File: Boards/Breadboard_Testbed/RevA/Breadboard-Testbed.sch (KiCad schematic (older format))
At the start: 13 parts, among them J1 main_conn_10, J10 Arduino-right, J11 Arduino-right, J12 Conn_02x12_Counter_Clockwise, J2 main_conn_12, J3 Conn_02x10_Counter_Clockwise, J4 Conn_02x10_Counter_Clockwise, J5 Conn_02x10_Counter_Clockwise, J6 Arduino-left, J7 Arduino-left, J8 Conn_02x10_Counter_Clockwise, J9 Conn_02x12_Counter_Clockwise

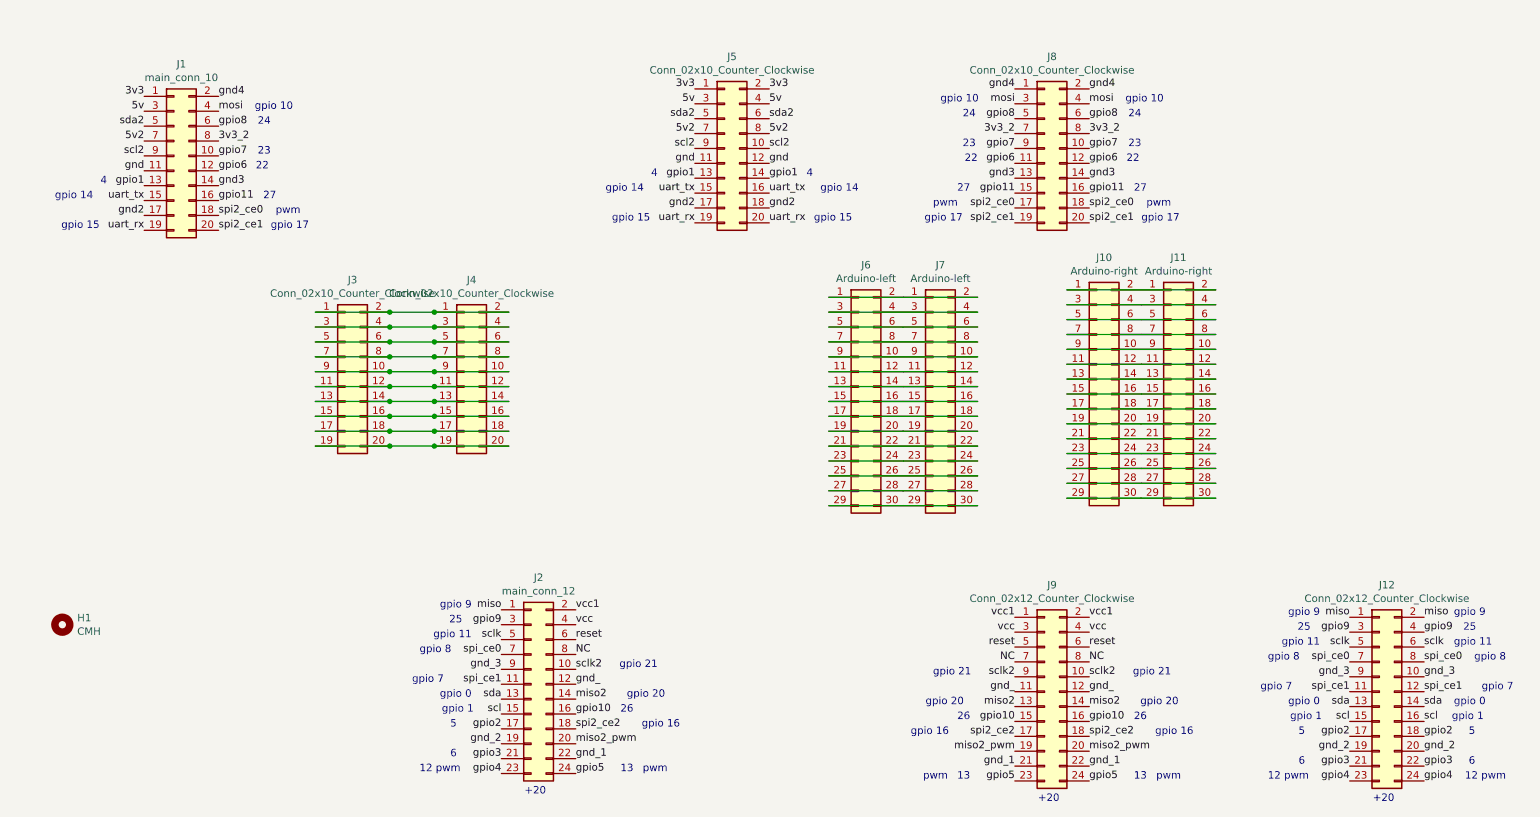
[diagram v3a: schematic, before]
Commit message: Finished Test-RevA layout Pre-route
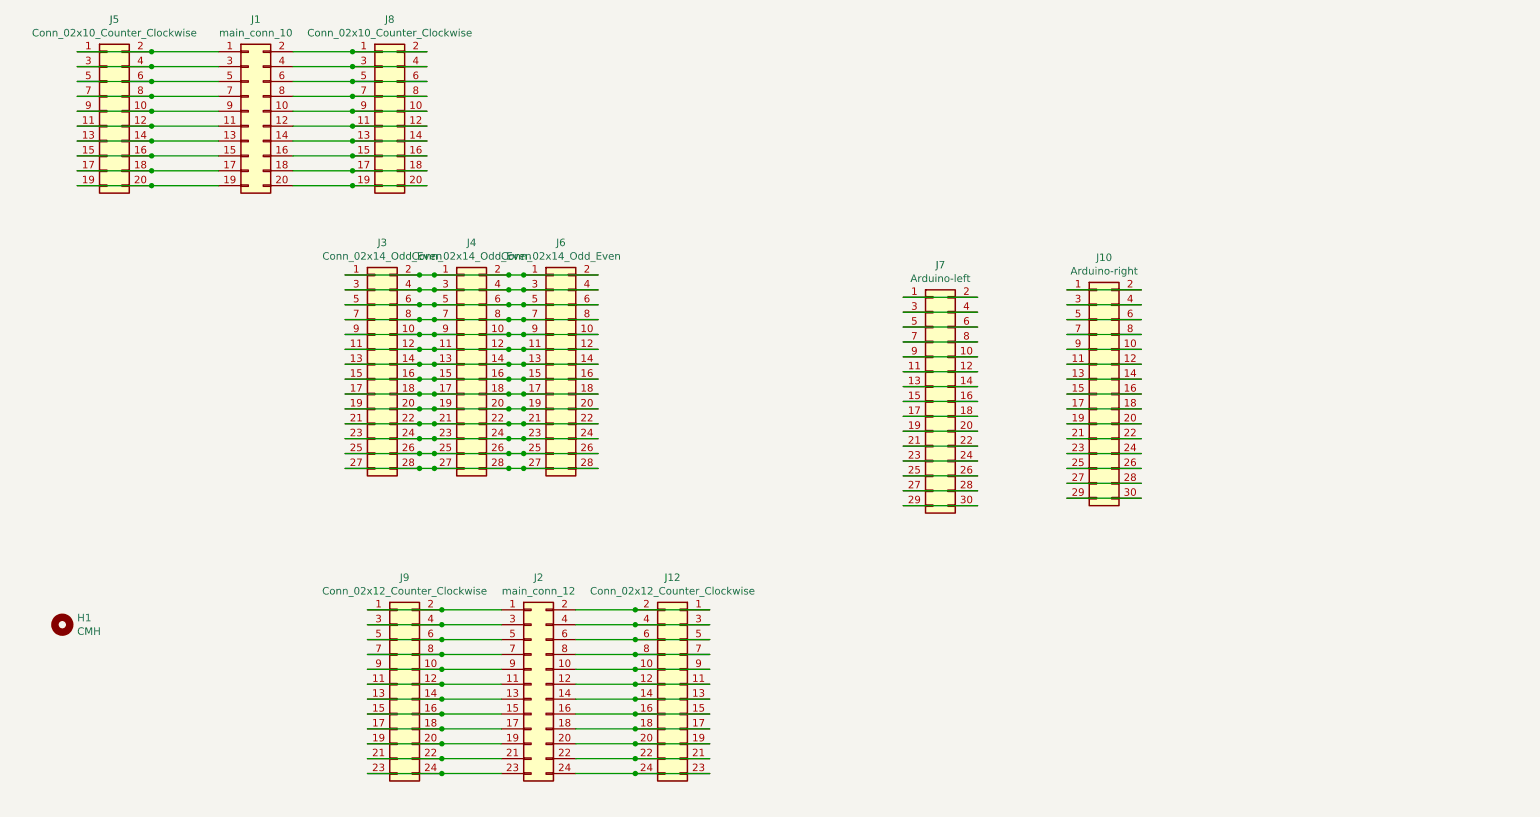
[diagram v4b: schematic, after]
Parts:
- removed J11: Arduino-right, Connector_PinHeader_2.54mm:PinHeader_2x15_P2.54mm_Vertical, symbol Connector_Generic:Conn_02x15_Odd_Even
- removed J3, J4: Conn_02x10_Counter_Clockwise, Connector_PinHeader_2.54mm:PinHeader_2x10_P2.54mm_Vertical, symbol Connector_Generic:Conn_02x10_Odd_Even
- removed J6: Arduino-left, Connector_PinHeader_2.54mm:PinHeader_2x15_P2.54mm_Vertical, symbol Connector_Generic:Conn_02x15_Odd_Even
- added J3, J4, J6: Conn_02x14_Odd_Even, Connector_PinHeader_2.54mm:PinHeader_2x14_P2.54mm_Vertical, symbol Connector_Generic:Conn_02x14_Odd_Even
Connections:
- net at J7.2 (Pin_2): now also J7.1 (Pin_1)
- net at J7.9 (Pin_9): now also J7.10 (Pin_10)
- net at J7.12 (Pin_12): now also J7.11 (Pin_11)
- net at J7.14 (Pin_14): now also J7.13 (Pin_13)
- net at J7.16 (Pin_16): now also J7.15 (Pin_15)
- net at J7.18 (Pin_18): now also J7.17 (Pin_17)
- net at J7.20 (Pin_20): now also J7.19 (Pin_19)
- net at J7.22 (Pin_22): now also J7.21 (Pin_21)
- net at J7.24 (Pin_24): now also J7.23 (Pin_23)
- net at J7.26 (Pin_26): now also J7.25 (Pin_25)
- net at J7.28 (Pin_28): now also J7.27 (Pin_27)
- net at J7.30 (Pin_30): now also J7.29 (Pin_29)
- net at J7.4 (Pin_4): now also J7.3 (Pin_3)
- net at J7.6 (Pin_6): now also J7.5 (Pin_5)
- net at J7.8 (Pin_8): now also J7.7 (Pin_7)
- net at J10.1 (Pin_1): now also J10.2 (Pin_2)
- net at J10.10 (Pin_10): now also J10.9 (Pin_9)
- net at J10.11 (Pin_11): now also J10.12 (Pin_12)
- net at J10.13 (Pin_13): now also J10.14 (Pin_14)
- net at J10.15 (Pin_15): now also J10.16 (Pin_16)
- net at J10.17 (Pin_17): now also J10.18 (Pin_18)
- net at J10.19 (Pin_19): now also J10.20 (Pin_20)
- net at J10.21 (Pin_21): now also J10.22 (Pin_22)
- net at J10.23 (Pin_23): now also J10.24 (Pin_24)
- net at J10.25 (Pin_25): now also J10.26 (Pin_26)
- net at J10.27 (Pin_27): now also J10.28 (Pin_28)
- net at J10.29 (Pin_29): now also J10.30 (Pin_30)
- net at J10.3 (Pin_3): now also J10.4 (Pin_4)
- net at J10.5 (Pin_5): now also J10.6 (Pin_6)
- net at J10.7 (Pin_7): now also J10.8 (Pin_8)
- net 3v3: no longer names the net of J1.1 (Pin_1), J5.1 (Pin_1), J5.2 (Pin_2)
- net 3v3_2: no longer names the net of J1.8 (Pin_8), J8.7 (Pin_7), J8.8 (Pin_8)
- net 5v: no longer names the net of J1.3 (Pin_3), J5.3 (Pin_3), J5.4 (Pin_4)
- net 5v2: no longer names the net of J1.7 (Pin_7), J5.7 (Pin_7), J5.8 (Pin_8)
- net NC: no longer names the net of J9.7 (Pin_7), J9.8 (Pin_8)
- net NC: now also J2.7 (Pin_7); no longer J2.8 (Pin_8)
- net gnd: no longer names the net of J1.11 (Pin_11), J5.11 (Pin_11), J5.12 (Pin_12)
- net gnd2: no longer names the net of J1.17 (Pin_17), J5.17 (Pin_17), J5.18 (Pin_18)
- net gnd3: no longer names the net of J1.14 (Pin_14), J8.13 (Pin_13), J8.14 (Pin_14)
- net gnd4: no longer names the net of J1.2 (Pin_2), J8.1 (Pin_1), J8.2 (Pin_2)
- net gnd_: no longer names the net of J9.11 (Pin_11), J9.12 (Pin_12)
- net gnd_: now also J2.11 (Pin_11); no longer J2.12 (Pin_12)
- net gnd_1: no longer names the net of J9.21 (Pin_21), J9.22 (Pin_22)
- net gnd_1: now also J2.21 (Pin_21); no longer J2.22 (Pin_22)
- net gnd_2: no longer names the net of J12.19 (Pin_19), J12.20 (Pin_20)
- net gnd_2: now also J2.20 (Pin_20); no longer J2.19 (Pin_19)
- net gnd_3: no longer names the net of J12.10 (Pin_10), J12.9 (Pin_9)
- net gnd_3: now also J2.10 (Pin_10); no longer J2.9 (Pin_9)
- net gpio1: no longer names the net of J1.13 (Pin_13), J5.13 (Pin_13), J5.14 (Pin_14)
- net gpio10: no longer names the net of J9.15 (Pin_15), J9.16 (Pin_16)
- net gpio10: now also J2.15 (Pin_15); no longer J2.16 (Pin_16)
- net gpio11: no longer names the net of J1.16 (Pin_16), J8.15 (Pin_15), J8.16 (Pin_16)
- net gpio2: no longer names the net of J12.17 (Pin_17), J12.18 (Pin_18)
- net gpio2: now also J2.18 (Pin_18); no longer J2.17 (Pin_17)
- net gpio3: no longer names the net of J12.21 (Pin_21), J12.22 (Pin_22)
- net gpio3: now also J2.22 (Pin_22); no longer J2.21 (Pin_21)
- net gpio4: no longer names the net of J12.23 (Pin_23), J12.24 (Pin_24)
- net gpio4: now also J2.24 (Pin_24); no longer J2.23 (Pin_23)
- net gpio5: no longer names the net of J9.23 (Pin_23), J9.24 (Pin_24)
- net gpio5: now also J2.23 (Pin_23); no longer J2.24 (Pin_24)
- net gpio6: no longer names the net of J1.12 (Pin_12), J8.11 (Pin_11), J8.12 (Pin_12)
- net gpio7: no longer names the net of J1.10 (Pin_10), J8.10 (Pin_10), J8.9 (Pin_9)
- net gpio8: no longer names the net of J1.6 (Pin_6), J8.5 (Pin_5), J8.6 (Pin_6)
- net gpio9: no longer names the net of J12.3 (Pin_3), J12.4 (Pin_4)
- net gpio9: now also J2.4 (Pin_4); no longer J2.3 (Pin_3)
- net miso: no longer names the net of J12.1 (Pin_1), J12.2 (Pin_2)
- net miso: now also J2.2 (Pin_2); no longer J2.1 (Pin_1)
- net miso2: no longer names the net of J9.13 (Pin_13), J9.14 (Pin_14)
- net miso2: now also J2.13 (Pin_13); no longer J2.14 (Pin_14)
- net miso2_pwm: no longer names the net of J9.19 (Pin_19), J9.20 (Pin_20)
- net miso2_pwm: now also J2.19 (Pin_19); no longer J2.20 (Pin_20)
- net mosi: no longer names the net of J1.4 (Pin_4), J8.3 (Pin_3), J8.4 (Pin_4)
- net reset: no longer names the net of J9.5 (Pin_5), J9.6 (Pin_6)
- net reset: now also J2.5 (Pin_5); no longer J2.6 (Pin_6)
- net scl: no longer names the net of J12.15 (Pin_15), J12.16 (Pin_16)
- net scl: now also J2.16 (Pin_16); no longer J2.15 (Pin_15)
- net scl2: no longer names the net of J1.9 (Pin_9), J5.10 (Pin_10), J5.9 (Pin_9)
- net sclk: no longer names the net of J12.5 (Pin_5), J12.6 (Pin_6)
- net sclk: now also J2.6 (Pin_6); no longer J2.5 (Pin_5)
- net sclk2: no longer names the net of J9.10 (Pin_10), J9.9 (Pin_9)
- net sclk2: now also J2.9 (Pin_9); no longer J2.10 (Pin_10)
- net sda: no longer names the net of J12.13 (Pin_13), J12.14 (Pin_14)
- net sda: now also J2.14 (Pin_14); no longer J2.13 (Pin_13)
- net sda2: no longer names the net of J1.5 (Pin_5), J5.5 (Pin_5), J5.6 (Pin_6)
- net spi2_ce0: no longer names the net of J1.18 (Pin_18), J8.17 (Pin_17), J8.18 (Pin_18)
- net spi2_ce1: no longer names the net of J1.20 (Pin_20), J8.19 (Pin_19), J8.20 (Pin_20)
- net spi2_ce2: no longer names the net of J9.17 (Pin_17), J9.18 (Pin_18)
- net spi2_ce2: now also J2.17 (Pin_17); no longer J2.18 (Pin_18)
- net spi_ce0: no longer names the net of J12.7 (Pin_7), J12.8 (Pin_8)
- net spi_ce0: now also J2.8 (Pin_8); no longer J2.7 (Pin_7)
- net spi_ce1: no longer names the net of J12.11 (Pin_11), J12.12 (Pin_12)
- net spi_ce1: now also J2.12 (Pin_12); no longer J2.11 (Pin_11)
- net uart_rx: no longer names the net of J1.19 (Pin_19), J5.19 (Pin_19), J5.20 (Pin_20)
- net uart_tx: no longer names the net of J1.15 (Pin_15), J5.15 (Pin_15), J5.16 (Pin_16)
- net vcc: no longer names the net of J9.3 (Pin_3), J9.4 (Pin_4)
- net vcc: now also J2.3 (Pin_3); no longer J2.4 (Pin_4)
- net vcc1: no longer names the net of J9.1 (Pin_1), J9.2 (Pin_2)
- net vcc1: now also J2.1 (Pin_1); no longer J2.2 (Pin_2)
- new net: J3.1 (Pin_1), J3.2 (Pin_2), J4.1 (Pin_1), J4.2 (Pin_2), J6.1 (Pin_1), J6.2 (Pin_2)
- new net: J3.10 (Pin_10), J3.9 (Pin_9), J4.10 (Pin_10), J4.9 (Pin_9), J6.10 (Pin_10), J6.9 (Pin_9)
- new net: J3.11 (Pin_11), J3.12 (Pin_12), J4.11 (Pin_11), J4.12 (Pin_12), J6.11 (Pin_11), J6.12 (Pin_12)
- new net: J3.13 (Pin_13), J3.14 (Pin_14), J4.13 (Pin_13), J4.14 (Pin_14), J6.13 (Pin_13), J6.14 (Pin_14)
- new net: J3.15 (Pin_15), J3.16 (Pin_16), J4.15 (Pin_15), J4.16 (Pin_16), J6.15 (Pin_15), J6.16 (Pin_16)
- new net: J3.17 (Pin_17), J3.18 (Pin_18), J4.17 (Pin_17), J4.18 (Pin_18), J6.17 (Pin_17), J6.18 (Pin_18)
- new net: J3.19 (Pin_19), J3.20 (Pin_20), J4.19 (Pin_19), J4.20 (Pin_20), J6.19 (Pin_19), J6.20 (Pin_20)
- new net: J3.21 (Pin_21), J3.22 (Pin_22), J4.21 (Pin_21), J4.22 (Pin_22), J6.21 (Pin_21), J6.22 (Pin_22)
- new net: J3.23 (Pin_23), J3.24 (Pin_24), J4.23 (Pin_23), J4.24 (Pin_24), J6.23 (Pin_23), J6.24 (Pin_24)
- new net: J3.25 (Pin_25), J3.26 (Pin_26), J4.25 (Pin_25), J4.26 (Pin_26), J6.25 (Pin_25), J6.26 (Pin_26)
- new net: J3.27 (Pin_27), J3.28 (Pin_28), J4.27 (Pin_27), J4.28 (Pin_28), J6.27 (Pin_27), J6.28 (Pin_28)
- new net: J3.3 (Pin_3), J3.4 (Pin_4), J4.3 (Pin_3), J4.4 (Pin_4), J6.3 (Pin_3), J6.4 (Pin_4)
- new net: J3.5 (Pin_5), J3.6 (Pin_6), J4.5 (Pin_5), J4.6 (Pin_6), J6.5 (Pin_5), J6.6 (Pin_6)
- new net: J3.7 (Pin_7), J3.8 (Pin_8), J4.7 (Pin_7), J4.8 (Pin_8), J6.7 (Pin_7), J6.8 (Pin_8)
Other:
- note removed: "+20"
- note removed: "12 pwm"
- note removed: "13"
- note removed: "22"
- note removed: "23"
- note removed: "24"
- note removed: "25"
- note removed: "26"
- note removed: "27"
- note removed: "4"
- note removed: "5"
- note removed: "6"
- note removed: "gpio 0"
- note removed: "gpio 1"
- note removed: "gpio 10"
- note removed: "gpio 11"
- note removed: "gpio 14"
- note removed: "gpio 15"
- note removed: "gpio 16"
- note removed: "gpio 17"
- note removed: "gpio 20"
- note removed: "gpio 21"
- note removed: "gpio 7"
- note removed: "gpio 8"
- note removed: "gpio 9"
- note removed: "pwm"
- moved on the sheet: J1, J5, J8, J9

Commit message: Testbed-RevA postroute complete
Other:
- moved on the sheet: J5, J8
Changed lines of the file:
@@
 L Connector_Generic:Conn_02x10_Odd_Even J5
 U 1 1 61FF84C4
-P 1450 1450
-F 0 "J5" H 1500 2067 50  0000 C CNN
-F 1 "Conn_02x10_Counter_Clockwise" H 1500 1976 50  0000 C CNN
-F 2 "Connector_PinHeader_2.54mm:PinHeader_2x10_P2.54mm_Vertical" H 1450 1450 50  0001 C CNN
-F 3 "~" H 1450 1450 50  0001 C CNN
-	1    1450 1450
+P 1900 1450
+F 0 "J5" H 1950 2067 50  0000 C CNN
+F 1 "Conn_02x10_Counter_Clockwise" H 1950 1976 50  0000 C CNN
+F 2 "Connector_PinHeader_2.54mm:PinHeader_2x10_P2.54mm_Vertical" H 1900 1450 50  0001 C CNN
+F 3 "~" H 1900 1450 50  0001 C CNN
+	1    1900 1450
 	1    0    0    -1
 $EndComp
@@
 $EndComp
 Wire Wire Line
-	2200 1050 1750 1050
-Wire Wire Line
-	1250 1050 1750 1050
-Connection ~ 1750 1050
-Wire Wire Line
-	2200 1150 1750 1150
-Wire Wire Line
-	1750 1150 1250 1150
-Connection ~ 1750 1150
-Wire Wire Line
-	1250 1250 1750 1250
-Wire Wire Line
-	2200 1250 1750 1250
-Connection ~ 1750 1250
-Wire Wire Line
-	2200 1350 1750 1350
-Wire Wire Line
-	1250 1350 1750 1350
-Connection ~ 1750 1350
-Wire Wire Line
-	1250 1450 1750 1450
-Wire Wire Line
-	1750 1450 2200 1450
-Connection ~ 1750 1450
-Wire Wire Line
-	2200 1550 1750 1550
-Wire Wire Line
-	1250 1550 1750 1550
-Connection ~ 1750 1550
-Wire Wire Line
-	1250 1650 1750 1650
-Wire Wire Line
-	1750 1650 2200 1650
-Connection ~ 1750 1650
-Wire Wire Line
-	2200 1750 1750 1750
-Wire Wire Line
-	1750 1750 1250 1750
-Connection ~ 1750 1750
-Wire Wire Line
-	1250 1850 1750 1850
-Wire Wire Line
-	1750 1850 2200 1850
-Connection ~ 1750 1850
-Wire Wire Line
-	2200 1950 1750 1950
-Wire Wire Line
-	1750 1950 1250 1950
-Connection ~ 1750 1950
+	1400 3050 900  3050
 $Comp
 L Connector_Generic:Conn_02x10_Odd_Even J8
 U 1 1 61FFAAA2
-P 3300 1450
-F 0 "J8" H 3350 2067 50  0000 C CNN
-F 1 "Conn_02x10_Counter_Clockwise" H 3350 1976 50  0000 C CNN
-F 2 "Connector_PinHeader_2.54mm:PinHeader_2x10_P2.54mm_Vertical" H 3300 1450 50  0001 C CNN
-F 3 "~" H 3300 1450 50  0001 C CNN
-	1    3300 1450
-	1    0    0    -1
-$EndComp
-Wire Wire Line
-	2700 1050 3100 1050
-Wire Wire Line
-	3600 1050 3100 1050
-Connection ~ 3100 1050
-Wire Wire Line
-	3600 1150 3100 1150
-Wire Wire Line
-	3100 1150 2700 1150
-Connection ~ 3100 1150
-Wire Wire Line
-	2700 1250 3100 1250
-Wire Wire Line
-	3600 1250 3100 1250
-Connection ~ 3100 1250
-Wire Wire Line
-	3600 1350 3100 1350
-Wire Wire Line
-	3100 1350 2700 1350
-Connection ~ 3100 1350
-Wire Wire Line
-	2700 1450 3100 1450
-Wire Wire Line
-	3100 1450 3600 1450
-Connection ~ 3100 1450
-Wire Wire Line
-	3600 1550 3100 1550
-Wire Wire Line
-	3100 1550 2700 1550
-Connection ~ 3100 1550
-Wire Wire Line
-	2700 1650 3100 1650
-Wire Wire Line
-	3100 1650 3600 1650
-Connection ~ 3100 1650
-Wire Wire Line
-	3600 1750 3100 1750
-Wire Wire Line
-	3100 1750 2700 1750
-Connection ~ 3100 1750
-Wire Wire Line
-	2700 1850 3100 1850
-Wire Wire Line
-	3600 1850 3100 1850
-Connection ~ 3100 1850
-Wire Wire Line
-	2700 1950 3100 1950
-Connection ~ 3100 1950
-Wire Wire Line
-	3100 1950 3600 1950
+P 2900 1450
+F 0 "J8" H 2950 2067 50  0000 C CNN
+F 1 "Conn_02x10_Counter_Clockwise" H 2950 1976 50  0000 C CNN
+F 2 "Connector_PinHeader_2.54mm:PinHeader_2x10_P2.54mm_Vertical" H 2900 1450 50  0001 C CNN
+F 3 "~" H 2900 1450 50  0001 C CNN
+	1    2900 1450
+	1    0    0    -1
+$EndComp
 Wire Wire Line
 	4100 4800 3700 4800
@@
 	3550 3850 3050 3850
 Connection ~ 3550 3850
+Wire Wire Line
+	2200 1050 1700 1050
+Connection ~ 2200 1050
+Wire Wire Line
+	2200 1150 1700 1150
+Connection ~ 2200 1150
+Wire Wire Line
+	1700 1250 2200 1250
+Connection ~ 2200 1250
+Wire Wire Line
+	2200 1350 1700 1350
+Connection ~ 2200 1350
+Wire Wire Line
+	1700 1450 2200 1450
+Connection ~ 2200 1450
+Wire Wire Line
+	2200 1550 1700 1550
+Connection ~ 2200 1550
+Wire Wire Line
+	1700 1650 2200 1650
+Connection ~ 2200 1650
+Wire Wire Line
+	2200 1750 1700 1750
+Connection ~ 2200 1750
+Wire Wire Line
+	1700 1850 2200 1850
+Connection ~ 2200 1850
+Wire Wire Line
+	2200 1950 1700 1950
+Connection ~ 2200 1950
+Wire Wire Line
+	2700 1950 3200 1950
+Connection ~ 2700 1950
+Wire Wire Line
+	3200 1850 2700 1850
+Connection ~ 2700 1850
+Wire Wire Line
+	2700 1750 3200 1750
+Connection ~ 2700 1750
+Wire Wire Line
+	3200 1650 2700 1650
+Connection ~ 2700 1650
+Wire Wire Line
+	2700 1550 3200 1550
+Connection ~ 2700 1550
+Wire Wire Line
+	3200 1450 2700 1450
+Connection ~ 2700 1450
+Wire Wire Line
+	2700 1350 3200 1350
+Connection ~ 2700 1350
+Wire Wire Line
+	3200 1250 2700 1250
+Connection ~ 2700 1250
+Wire Wire Line
+	2700 1150 3200 1150
+Connection ~ 2700 1150
+Wire Wire Line
+	3200 1050 2700 1050
+Connection ~ 2700 1050
 $EndSCHEMATC
